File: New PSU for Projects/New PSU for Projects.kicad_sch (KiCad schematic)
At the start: 40 parts, among them IC4 LF351DT, J1 Toroid 5VA/15V, J2 240V Mains, Q1 BC848, Q2 BC848, U3 SN74HC74N

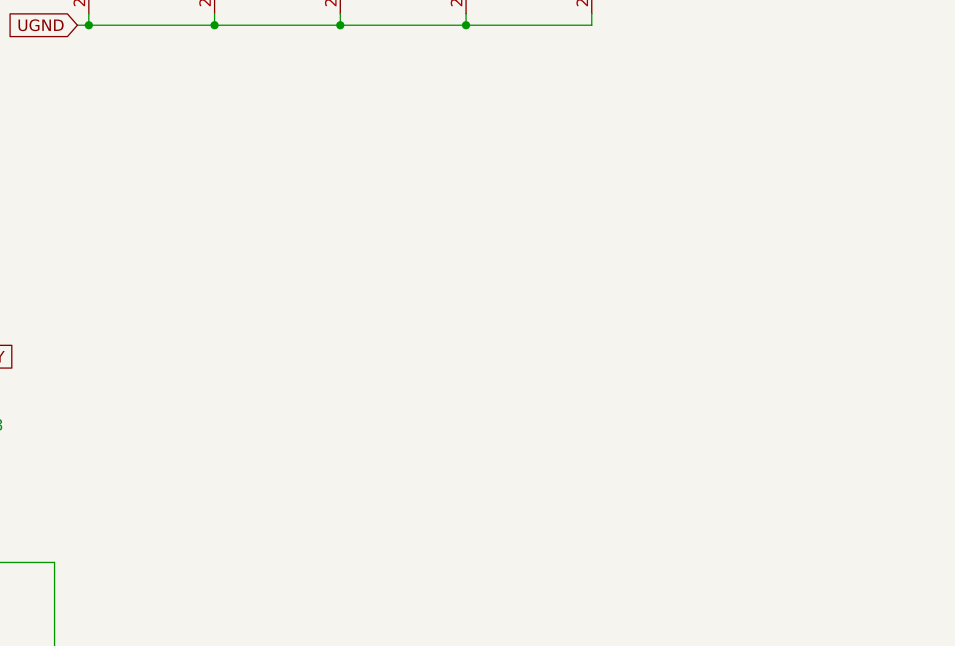
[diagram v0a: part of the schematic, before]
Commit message: Swapped out Op-Amp for a Comparator
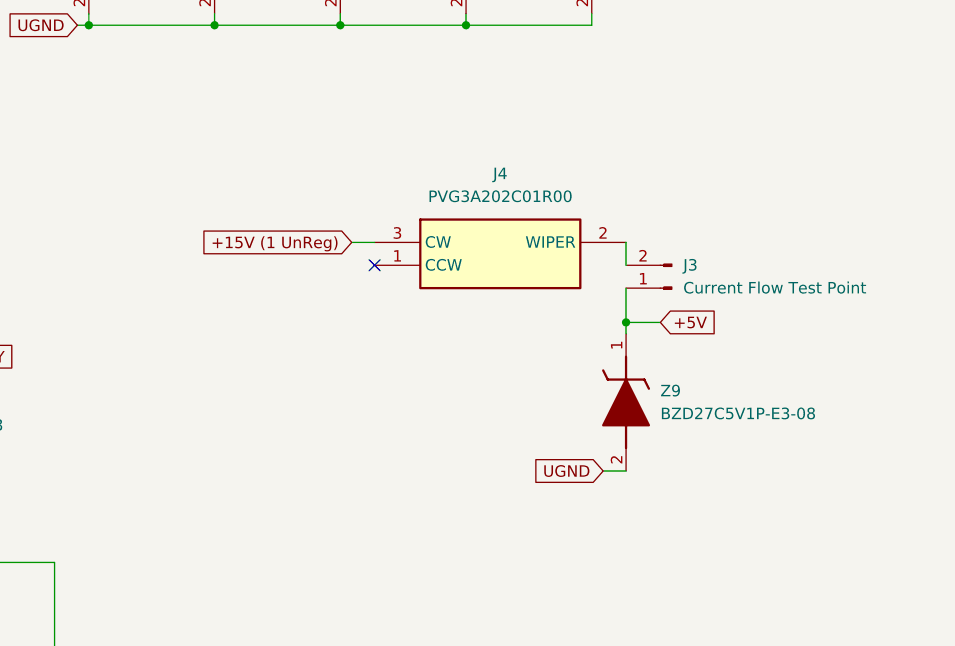
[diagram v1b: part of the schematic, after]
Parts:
- added J3: Current Flow Test Point, symbol Connector:Conn_01x02_Pin
- added J4: PVG3A202C01R00, PVG3A202C01R00, symbol SamacSys_Parts:PVG3A202C01R00
- added Z9: BZD27C5V1P-E3-08, SODFL3718X108N, symbol SamacSys_Parts:BZD27C5V1P-E3-08
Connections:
- net +15V (1 UnReg): now also J4.3 (CW)
- net +5V: now also J3.1 (Pin_1), Z9.1 (K)
- net UGND: now also Z9.2 (A)
- new net: J3.2 (Pin_2), J4.2 (WIPER)
- no-connect marks 3 -> 4
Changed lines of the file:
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@@
   (junction (at 35.56 144.78) (diameter 0) (color 0 0 0 0)
+  )
+  (junction (at 196.85 100.33) (diameter 0) (color 0 0 0 0)
   )
   (junction (at 137.16 33.02) (diameter 0) (color 0 0 0 0)
@@
   (no_connect (at 120.65 147.32))
   (no_connect (at 41.91 57.15))
+  (no_connect (at 168.91 93.98))
   (wire (pts (xy 60.96 170.18) (xy 63.5 170.18))
     (stroke (width 0) (type default))
@@
     (stroke (width 0) (type default))
   )
+  (wire (pts (xy 196.85 96.52) (xy 196.85 100.33))
+    (stroke (width 0) (type default))
+  )
   (wire (pts (xy 95.25 43.18) (xy 97.79 43.18))
     (stroke (width 0) (type default))
@@
     (stroke (width 0) (type default))
   )
+  (wire (pts (xy 200.66 100.33) (xy 196.85 100.33))
+    (stroke (width 0) (type default))
+  )
   (wire (pts (xy 72.39 162.56) (xy 76.2 162.56))
     (stroke (width 0) (type default))
@@
     (stroke (width 0) (type default))
   )
+  (wire (pts (xy 194.31 116.84) (xy 196.85 116.84))
+    (stroke (width 0) (type default))
+  )
   (wire (pts (xy 72.39 190.5) (xy 76.2 190.5))
     (stroke (width 0) (type default))
@@
     (stroke (width 0) (type default))
   )
+  (wire (pts (xy 166.37 91.44) (xy 168.91 91.44))
+    (stroke (width 0) (type default))
+  )
   (wire (pts (xy 36.83 40.64) (xy 41.91 40.64))
     (stroke (width 0) (type default))
@@
     (stroke (width 0) (type default))
   )
+  (wire (pts (xy 196.85 91.44) (xy 196.85 93.98))
+    (stroke (width 0) (type default))
+  )
   (wire (pts (xy 40.64 119.38) (xy 41.91 119.38))
     (stroke (width 0) (type default))
@@
   )
   (wire (pts (xy 179.07 33.02) (xy 165.1 33.02))
+    (stroke (width 0) (type default))
+  )
+  (wire (pts (xy 196.85 100.33) (xy 196.85 101.6))
     (stroke (width 0) (type default))
   )
@@
     )
   )
+  (global_label "+15V (1 UnReg)" (shape input) (at 166.37 91.44 180) (fields_autoplaced)
+    (effects (font (size 1.27 1.27)) (justify right))
+    (property "Intersheetrefs" "${INTERSHEET_REFS}" (at 147.4796 91.44 0)
+      (effects (font (size 1.27 1.27)) (justify right) hide)
+    )
+  )
   (global_label "1MHz INV" (shape input) (at 83.82 180.34 0) (fields_autoplaced)
     (effects (font (size 1.27 1.27)) (justify left))
@@
     )
   )
+  (global_label "+5V" (shape input) (at 200.66 100.33 0) (fields_autoplaced)
+    (effects (font (size 1.27 1.27)) (justify left))
+    (property "Intersheetrefs" "${INTERSHEET_REFS}" (at 207.5157 100.33 0)
+      (effects (font (size 1.27 1.27)) (justify left) hide)
+    )
+  )
   (global_label "UGND" (shape input) (at 41.91 87.63 90) (fields_autoplaced)
     (effects (font (size 1.27 1.27)) (justify left))
@@
     (effects (font (size 1.27 1.27)) (justify right))
     (property "Intersheetrefs" "${INTERSHEET_REFS}" (at 54.6764 180.2606 0)
+      (effects (font (size 1.27 1.27)) (justify right) hide)
+    )
+  )
+  (global_label "UGND" (shape input) (at 194.31 116.84 180) (fields_autoplaced)
+    (effects (font (size 1.27 1.27)) (justify right))
+    (property "Intersheetrefs" "${INTERSHEET_REFS}" (at 186.1238 116.84 0)
       (effects (font (size 1.27 1.27)) (justify right) hide)
     )
@@
     )
   )
+  (symbol (lib_id "SamacSys_Parts:BZD27C5V1P-E3-08") (at 196.85 101.6 270) (unit 1)
+    (in_bom yes) (on_board yes) (dnp no) (fields_autoplaced)
+    (property "Reference" "Z9" (at 200.66 107.95 90)
+      (effects (font (size 1.27 1.27)) (justify left))
+    )
+    (property "Value" "BZD27C5V1P-E3-08" (at 200.66 110.49 90)
+      (effects (font (size 1.27 1.27)) (justify left))
+    )
+    (property "Footprint" "SODFL3718X108N" (at 103.2 111.76 0)
+      (effects (font (size 1.27 1.27)) (justify left top) hide)
+    )
+    (property "Datasheet" "https://www.vishay.com/docs/85153/bzd27series.pdf" (at 3.2 111.76 0)
+      (effects (font (size 1.27 1.27)) (justify left top) hide)
+    )
+    (property "Height" "1.08" (at -196.8 111.76 0)
+      (effects (font (size 1.27 1.27)) (justify left top) hide)
+    )
+    (property "element14 Part Number" "" (at -296.8 111.76 0)
+      (effects (font (size 1.27 1.27)) (justify left top) hide)
+    )
+    (property "element14 Price/Stock" "" (at -396.8 111.76 0)
+      (effects (font (size 1.27 1.27)) (justify left top) hide)
+    )
+    (property "Manufacturer_Name" "Vishay" (at -496.8 111.76 0)
+      (effects (font (size 1.27 1.27)) (justify left top) hide)
+    )
+    (property "Manufacturer_Part_Number" "BZD27C5V1P-E3-08" (at -596.8 111.76 0)
+      (effects (font (size 1.27 1.27)) (justify left top) hide)
+    )
+    (pin "1")
+    (pin "2")
+    (instances
+      (project "New PSU for Projects"
+        (path "/85fd2437-e05d-4e79-b382-54f944530ebe"
+          (reference "Z9") (unit 1)
+        )
+      )
+    )
+  )
   (symbol (lib_id "EEE-1HA221P:EEE-1HA221P") (at 165.1 58.42 270) (unit 1)
     (in_bom yes) (on_board yes) (dnp no) (fields_autoplaced)
@@
         (path "/85fd2437-e05d-4e79-b382-54f944530ebe"
           (reference "R4") (unit 1)
+        )
+      )
+    )
+  )
+  (symbol (lib_id "SamacSys_Parts:PVG3A202C01R00") (at 168.91 91.44 0) (unit 1)
+    (in_bom yes) (on_board yes) (dnp no) (fields_autoplaced)
+    (property "Reference" "J4" (at 182.88 83.82 0)
+      (effects (font (size 1.27 1.27)))
+    )
+    (property "Value" "PVG3A202C01R00" (at 182.88 86.36 0)
+      (effects (font (size 1.27 1.27)))
+    )
+    (property "Footprint" "PVG3A202C01R00" (at 193.04 186.36 0)
+      (effects (font (size 1.27 1.27)) (justify left top) hide)
+    )
+    (property "Datasheet" "https://datasheet.datasheetarchive.com/originals/distributors/Datasheets_SAMA/db4b10663a027a846805e39c0e426696.pdf" (at 193.04 286.36 0)
+      (effects (font (size 1.27 1.27)) (justify left top) hide)
+    )
+    (property "Height" "2" (at 193.04 486.36 0)
+      (effects (font (size 1.27 1.27)) (justify left top) hide)
+    )
+    (property "element14 Part Number" "" (at 193.04 586.36 0)
+      (effects (font (size 1.27 1.27)) (justify left top) hide)
+    )
+    (property "element14 Price/Stock" "" (at 193.04 686.36 0)
+      (effects (font (size 1.27 1.27)) (justify left top) hide)
+    )
+    (property "Manufacturer_Name" "Bourns" (at 193.04 786.36 0)
+      (effects (font (size 1.27 1.27)) (justify left top) hide)
+    )
+    (property "Manufacturer_Part_Number" "PVG3A202C01R00" (at 193.04 886.36 0)
+      (effects (font (size 1.27 1.27)) (justify left top) hide)
+    )
+    (pin "1")
+    (pin "2")
+    (pin "3")
+    (instances
+      (project "New PSU for Projects"
+        (path "/85fd2437-e05d-4e79-b382-54f944530ebe"
+          (reference "J4") (unit 1)
         )
       )
@@
         )
       )
+    )
+  )
+  (symbol (lib_id "Connector:Conn_01x02_Pin") (at 201.93 96.52 180) (unit 1)
+    (in_bom yes) (on_board yes) (dnp no) (fields_autoplaced)
+    (property "Reference" "J3" (at 203.2 93.98 0)
+      (effects (font (size 1.27 1.27)) (justify right))
+    )
+    (property "Value" "Current Flow Test Point" (at 203.2 96.52 0)
+      (effects (font (size 1.27 1.27)) (justify right))
+    )
+    (property "Footprint" "" (at 201.93 96.52 0)
+      (effects (font (size 1.27 1.27)) hide)
+    )
+    (property "Datasheet" "~" (at 201.93 96.52 0)
+      (effects (font (size 1.27 1.27)) hide)
+    )
+    (pin "1")
+    (pin "2")
+    (instances
+      (project "New PSU for Projects"
+        (path "/85fd2437-e05d-4e79-b382-54f944530ebe"
+          (reference "J3") (unit 1)
+        )
+      )

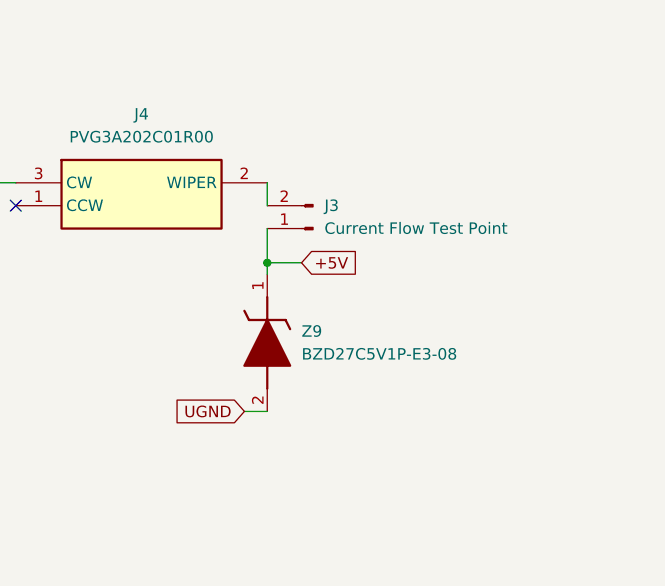
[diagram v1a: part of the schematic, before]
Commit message: Minor Change to feedback circuit
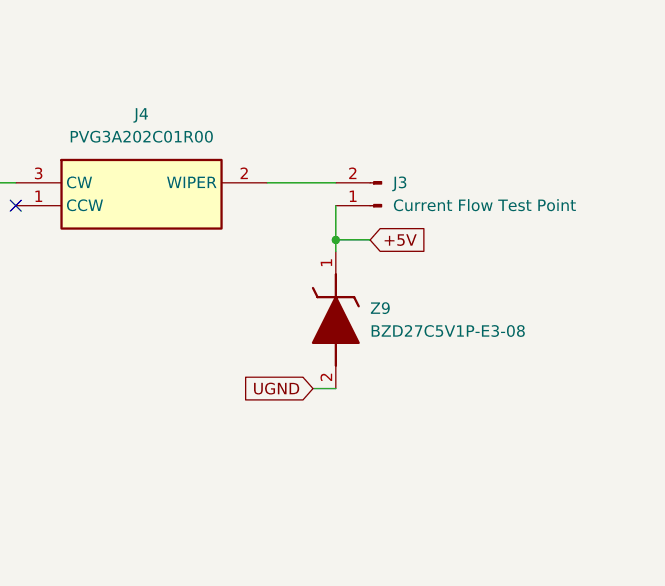
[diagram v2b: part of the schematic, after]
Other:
- moved on the sheet: J3, Z9
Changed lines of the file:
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@@
   (junction (at 35.56 144.78) (diameter 0) (color 0 0 0 0)
   )
-  (junction (at 196.85 100.33) (diameter 0) (color 0 0 0 0)
+  (junction (at 204.47 97.79) (diameter 0) (color 0 0 0 0)
   )
   (junction (at 137.16 33.02) (diameter 0) (color 0 0 0 0)
@@
     (stroke (width 0) (type default))
   )
-  (wire (pts (xy 196.85 96.52) (xy 196.85 100.33))
+  (wire (pts (xy 204.47 93.98) (xy 204.47 97.79))
     (stroke (width 0) (type default))
   )
@@
     (stroke (width 0) (type default))
   )
-  (wire (pts (xy 200.66 100.33) (xy 196.85 100.33))
+  (wire (pts (xy 208.28 97.79) (xy 204.47 97.79))
     (stroke (width 0) (type default))
   )
@@
     (stroke (width 0) (type default))
   )
-  (wire (pts (xy 194.31 116.84) (xy 196.85 116.84))
+  (wire (pts (xy 201.93 114.3) (xy 204.47 114.3))
     (stroke (width 0) (type default))
   )
@@
     (stroke (width 0) (type default))
   )
+  (wire (pts (xy 196.85 91.44) (xy 204.47 91.44))
+    (stroke (width 0) (type default))
+  )
   (wire (pts (xy 179.07 33.02) (xy 179.07 34.29))
     (stroke (width 0) (type default))
@@
     (stroke (width 0) (type default))
   )
-  (wire (pts (xy 196.85 91.44) (xy 196.85 93.98))
-    (stroke (width 0) (type default))
-  )
   (wire (pts (xy 40.64 119.38) (xy 41.91 119.38))
     (stroke (width 0) (type default))
@@
     (stroke (width 0) (type default))
   )
-  (wire (pts (xy 196.85 100.33) (xy 196.85 101.6))
+  (wire (pts (xy 204.47 97.79) (xy 204.47 99.06))
     (stroke (width 0) (type default))
   )
@@
     )
   )
-  (global_label "+5V" (shape input) (at 200.66 100.33 0) (fields_autoplaced)
+  (global_label "+5V" (shape input) (at 208.28 97.79 0) (fields_autoplaced)
     (effects (font (size 1.27 1.27)) (justify left))
-    (property "Intersheetrefs" "${INTERSHEET_REFS}" (at 207.5157 100.33 0)
+    (property "Intersheetrefs" "${INTERSHEET_REFS}" (at 215.1357 97.79 0)
       (effects (font (size 1.27 1.27)) (justify left) hide)
     )
@@
     )
   )
-  (global_label "UGND" (shape input) (at 194.31 116.84 180) (fields_autoplaced)
-    (effects (font (size 1.27 1.27)) (justify right))
-    (property "Intersheetrefs" "${INTERSHEET_REFS}" (at 186.1238 116.84 0)
+  (global_label "UGND" (shape input) (at 201.93 114.3 180) (fields_autoplaced)
+    (effects (font (size 1.27 1.27)) (justify right))
+    (property "Intersheetrefs" "${INTERSHEET_REFS}" (at 193.7438 114.3 0)
       (effects (font (size 1.27 1.27)) (justify right) hide)
     )
@@
     )
   )
-  (symbol (lib_id "SamacSys_Parts:BZD27C5V1P-E3-08") (at 196.85 101.6 270) (unit 1)
-    (in_bom yes) (on_board yes) (dnp no) (fields_autoplaced)
-    (property "Reference" "Z9" (at 200.66 107.95 90)
+  (symbol (lib_id "SamacSys_Parts:BZD27C5V1P-E3-08") (at 204.47 99.06 270) (unit 1)
+    (in_bom yes) (on_board yes) (dnp no) (fields_autoplaced)
+    (property "Reference" "Z9" (at 208.28 105.41 90)
       (effects (font (size 1.27 1.27)) (justify left))
     )
-    (property "Value" "BZD27C5V1P-E3-08" (at 200.66 110.49 90)
+    (property "Value" "BZD27C5V1P-E3-08" (at 208.28 107.95 90)
       (effects (font (size 1.27 1.27)) (justify left))
     )
-    (property "Footprint" "SODFL3718X108N" (at 103.2 111.76 0)
-      (effects (font (size 1.27 1.27)) (justify left top) hide)
-    )
-    (property "Datasheet" "https://www.vishay.com/docs/85153/bzd27series.pdf" (at 3.2 111.76 0)
-      (effects (font (size 1.27 1.27)) (justify left top) hide)
-    )
-    (property "Height" "1.08" (at -196.8 111.76 0)
-      (effects (font (size 1.27 1.27)) (justify left top) hide)
-    )
-    (property "element14 Part Number" "" (at -296.8 111.76 0)
-      (effects (font (size 1.27 1.27)) (justify left top) hide)
-    )
-    (property "element14 Price/Stock" "" (at -396.8 111.76 0)
-      (effects (font (size 1.27 1.27)) (justify left top) hide)
-    )
-    (property "Manufacturer_Name" "Vishay" (at -496.8 111.76 0)
-      (effects (font (size 1.27 1.27)) (justify left top) hide)
-    )
-    (property "Manufacturer_Part_Number" "BZD27C5V1P-E3-08" (at -596.8 111.76 0)
+    (property "Footprint" "SODFL3718X108N" (at 110.82 109.22 0)
+      (effects (font (size 1.27 1.27)) (justify left top) hide)
+    )
+    (property "Datasheet" "https://www.vishay.com/docs/85153/bzd27series.pdf" (at 10.82 109.22 0)
+      (effects (font (size 1.27 1.27)) (justify left top) hide)
+    )
+    (property "Height" "1.08" (at -189.18 109.22 0)
+      (effects (font (size 1.27 1.27)) (justify left top) hide)
+    )
+    (property "element14 Part Number" "" (at -289.18 109.22 0)
+      (effects (font (size 1.27 1.27)) (justify left top) hide)
+    )
+    (property "element14 Price/Stock" "" (at -389.18 109.22 0)
+      (effects (font (size 1.27 1.27)) (justify left top) hide)
+    )
+    (property "Manufacturer_Name" "Vishay" (at -489.18 109.22 0)
+      (effects (font (size 1.27 1.27)) (justify left top) hide)
+    )
+    (property "Manufacturer_Part_Number" "BZD27C5V1P-E3-08" (at -589.18 109.22 0)
       (effects (font (size 1.27 1.27)) (justify left top) hide)
     )
@@
     )
   )
-  (symbol (lib_id "Connector:Conn_01x02_Pin") (at 201.93 96.52 180) (unit 1)
-    (in_bom yes) (on_board yes) (dnp no) (fields_autoplaced)
-    (property "Reference" "J3" (at 203.2 93.98 0)
-      (effects (font (size 1.27 1.27)) (justify right))
-    )
-    (property "Value" "Current Flow Test Point" (at 203.2 96.52 0)
-      (effects (font (size 1.27 1.27)) (justify right))
-    )
-    (property "Footprint" "" (at 201.93 96.52 0)
-      (effects (font (size 1.27 1.27)) hide)
-    )
-    (property "Datasheet" "~" (at 201.93 96.52 0)
-      (effects (font (size 1.27 1.27)) hide)
-    )
+  (symbol (lib_id "Connector:Conn_01x02_Pin") (at 209.55 93.98 180) (unit 1)
+    (in_bom yes) (on_board yes) (dnp no) (fields_autoplaced)
+    (property "Reference" "J3" (at 210.82 91.44 0)
+      (effects (font (size 1.27 1.27)) (justify right))
+    )
+    (property "Value" "Current Flow Test Point" (at 210.82 93.98 0)
+      (effects (font (size 1.27 1.27)) (justify right))
+    )
+    (property "Footprint" "" (at 209.55 93.98 0)
+      (effects (font (size 1.27 1.27)) hide)
+    )
+    (property "Datasheet" "~" (at 209.55 93.98 0)
+      (effects (font (size 1.27 1.27)) hide)
+    )

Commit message: A few minor changes
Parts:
- removed D5, D6, D7, D8: B340, Diode_SMD:D_SMC, symbol Diode:B340
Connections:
- net +15V (2 UnReg) is gone; now on net BLK: C10.1, C3.1, C4.1, C6.1, C9.1
- net ORA is gone; now on net BLK: J1.4 (Pin_4)
- net +15V (1 UnReg): now also D2.1 (K); no longer D1.1 (K)
- net BLK: now also C1.2, C13.2, C14.2, C2.2, C3.1, C5.1, C5.2, C7.2, C8.2, IC4.4 (VCC-), Q1.2 (E), Q2.2 (E), R2.1, U3.7 (GND), Z9.2 (A); no longer D3.1 (K), D4.2 (A)
- net RED: now also D1.1 (K), D2.2 (A); no longer D1.2 (A), D2.1 (K)
- net YEL: now also D3.1 (K), D4.2 (A)
- removed net UGND: C1.2, C10.2, C13.2, C14.2, C2.2, C3.1, C3.2, C4.2, C5.1, C5.2, C6.2, C7.2, C8.2, C9.2, D2.2 (A), D3.2 (A), IC4.4 (VCC-), Q1.2 (E), Q2.2 (E), R2.1, U3.7 (GND), Z9.2 (A)
- new net -15V (2 UnReg): C10.2, C3.2, C4.2, C6.2, C9.2, D1.2 (A), D3.2 (A)
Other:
- moved on the sheet: C1, C10, C2, C3, C4, C5, C6, C7, C8, C9, D1, D2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

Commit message: Lyrebird Initial Upload
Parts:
- added C39 (x2): 100nF, Capacitor_SMD:C_1206_3216Metric, symbol Device:C_Small
- added C39 (x2): 390nF, Capacitor_SMD:C_1206_3216Metric, symbol Device:C_Small
- added C39 (x2): 220nF, Capacitor_SMD:C_1206_3216Metric, symbol Device:C_Small
- added D11, D13: US1M-E3_5AT, DIOM5127X229N, symbol SamacSys_Parts:US1M-E3_5AT
- added IC5: AZV3002S-13, SOIC127P600X175-8N, symbol SamacSys_Parts:AZV3002S-13
- added L1, L2: 784325042, INDPM105100X463N, symbol SamacSys_Parts:784325042
- added Q3, Q4: BC848, Package_TO_SOT_SMD:SOT-23, symbol Transistor_BJT:BC848
- added Q4, Q5: IRFR2905ZTRPBF, IRFR2905ZTRPBF, symbol SamacSys_Parts:IRFR2905ZTRPBF
- added R10 (x4): 10k, Resistor_SMD:R_1206_3216Metric, symbol Device:R
- added R77, R78: 10R, Resistor_SMD:R_1206_3216Metric, symbol Device:R
- added VR1, VR2: 3224W-1-504E, 3224W1205E, symbol SamacSys_Parts:3224W-1-504E
- J1: value Toroid 5VA/15V -> Toroid 15VA/9V
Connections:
- net +15V (1 UnReg): now also Q5.2 (D)
- net +5V: now also IC5.8 (VCC), R10.2, R10.2, VR1.3 (CW), VR2.3 (CW)
- net -15V (2 UnReg): now also Q4.3 (S)
- net BLK: now also C39.1, C39.1, C39.1, C39.2, C39.2, C39.2, IC5.4 (GND), Q3.2 (E), Q4.2 (E), VR1.1 (CCW), VR2.1 (CCW)
- net TRI WAVE OUT: now also IC5.3 (INPUT1+), IC5.5 (INPUT2+)
- net INV 1A: no longer names the net of C14.1, R10.1, R10.2, XTAL1.2
- new net: Q3.1 (B), R10.2
- new net: D11.2 (A), Q4.1 (G), R78.1
- new net: L2.1, Q4.2 (D)
- new net: D11.1 (K), R78.2
- new net: D13.1 (K), R77.2
- new net: D13.2 (A), Q5.1 (G), R77.1
- new net: L1.1, Q5.3 (S)
- new net: Q4.1 (B), R10.2
- new net +12V: C39.2, C39.2, C39.2, L1.2
- new net +IVE Control: IC5.1 (OUTPUT1), R10.1
- new net +IVE Drive: Q3.3 (C), R10.1
- new net +IVE FeedBack: IC5.2 (INPUT1-)
- new net +IVE Set: VR1.2 (WIPER)
- new net -12V: C39.1, C39.1, C39.1, L2.2
- new net -NEG Control: IC5.7 (OUTPUT2), R10.1
- new net -NEG Drive: Q4.3 (C), R10.1
- new net -NEG FeedBack: IC5.6 (INPUT2-)
- new net -NEG Set: VR2.2 (WIPER)
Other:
- removed sheet PSU Output
- moved on the sheet: C1, C10, C13, C14, C2, C3, C4, C5, C6, C7, C8, C9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
